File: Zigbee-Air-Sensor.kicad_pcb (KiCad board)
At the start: 4 copper layers, 34 x 45 mm, 87 parts, among them J1 USB_C_Receptacle_PowerOnly_6P, J2 Conn_01x04, J3 FH34SRJ-6S-0.5SH, J4 FH34SRJ-6S-0.5SH, J5 Conn_01x06, J6 E-Ink 24P, Q1 BC847W, Q2 CJ2101, Q3 Si1308EDL, U1 ESP32-H2-MINI-1-H4, U2 BQ25628ERYKR, U3 BQ27426YZFR, U4 TPS63030DSK, U5 SHT30-DIS, U6 LPS22DF

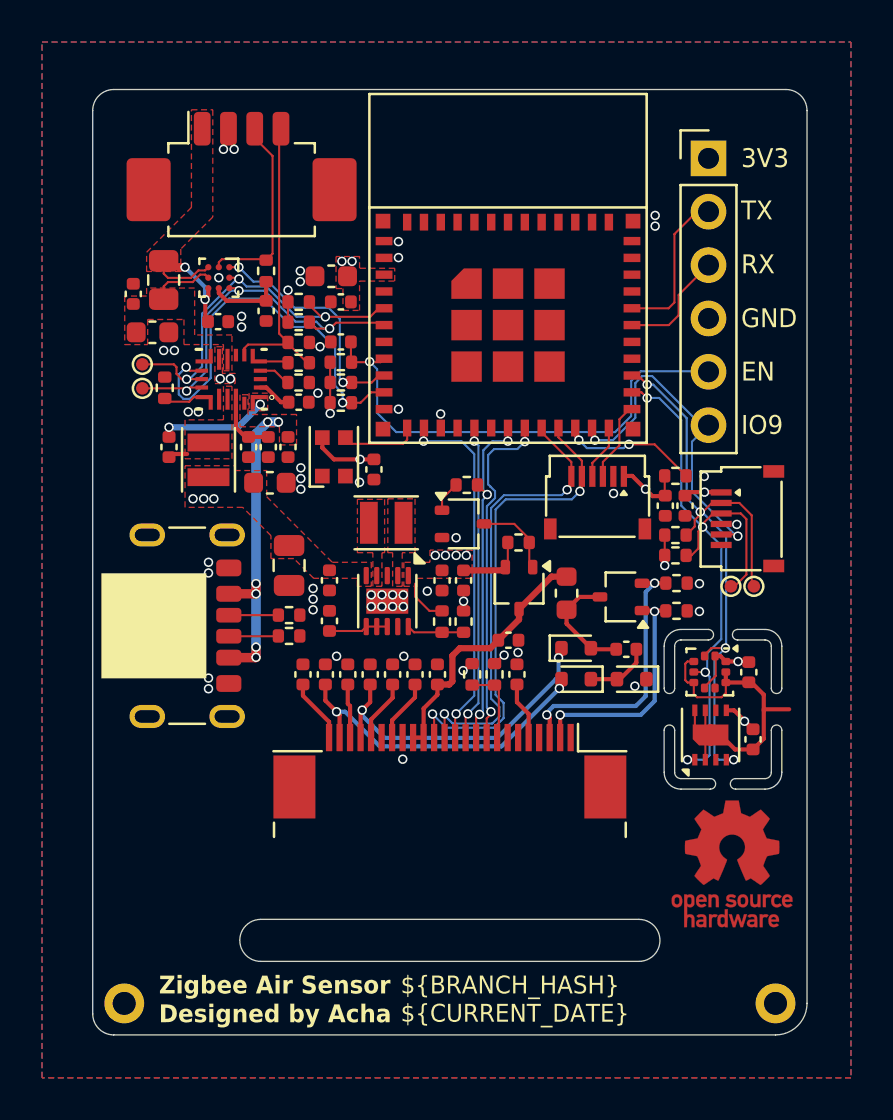
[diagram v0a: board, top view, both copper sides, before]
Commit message: Change non-plated slots to plated slots
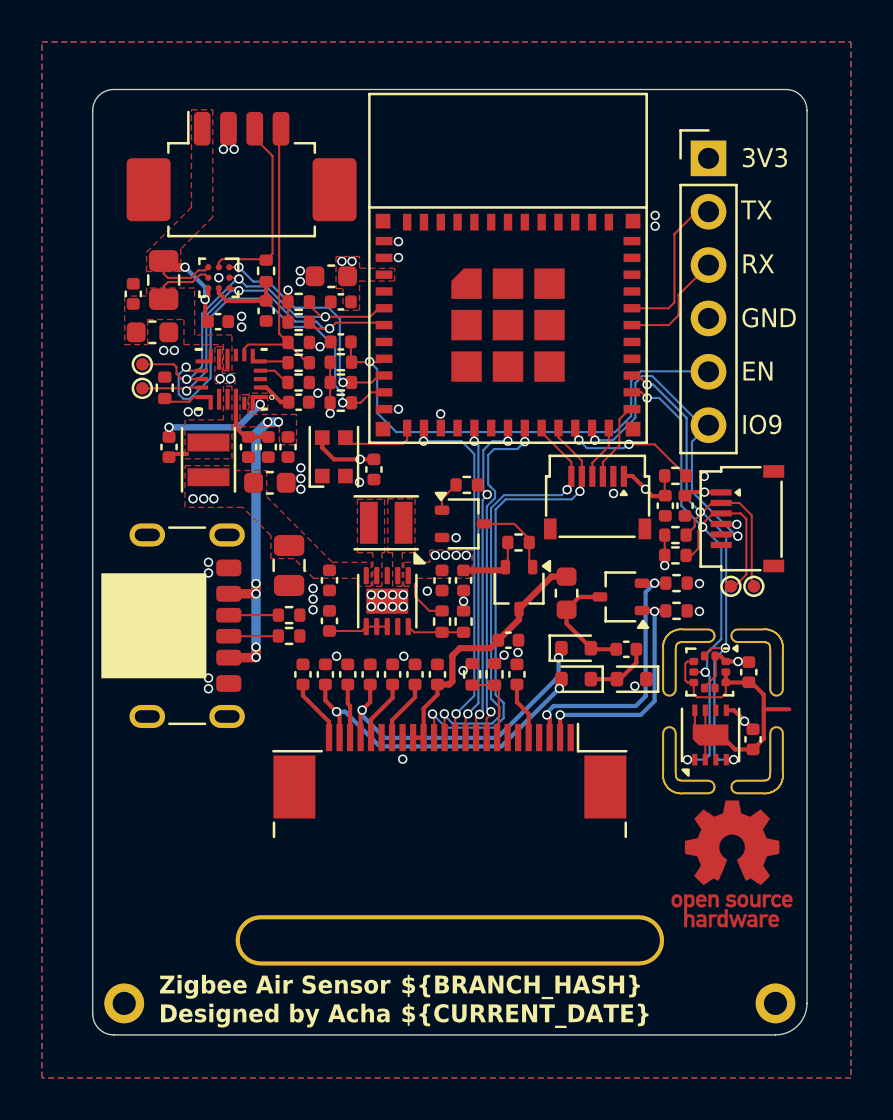
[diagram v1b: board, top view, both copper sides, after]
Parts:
- added 20.4mm_Plated_Slot: , Zigbee-Air-Sensor:20.4mm_Plated_Slot, F.Cu at (117.0, 140.5)
- added Thermal_Slot: Thermal_Slot, Zigbee-Air-Sensor:Thermal_Slot, F.Cu at (130.0, 129.6)
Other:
- outline, holes or cut-outs redrawn
- board text added: "Plated Slot"

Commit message: Adjust slot size Change GPIO assignment
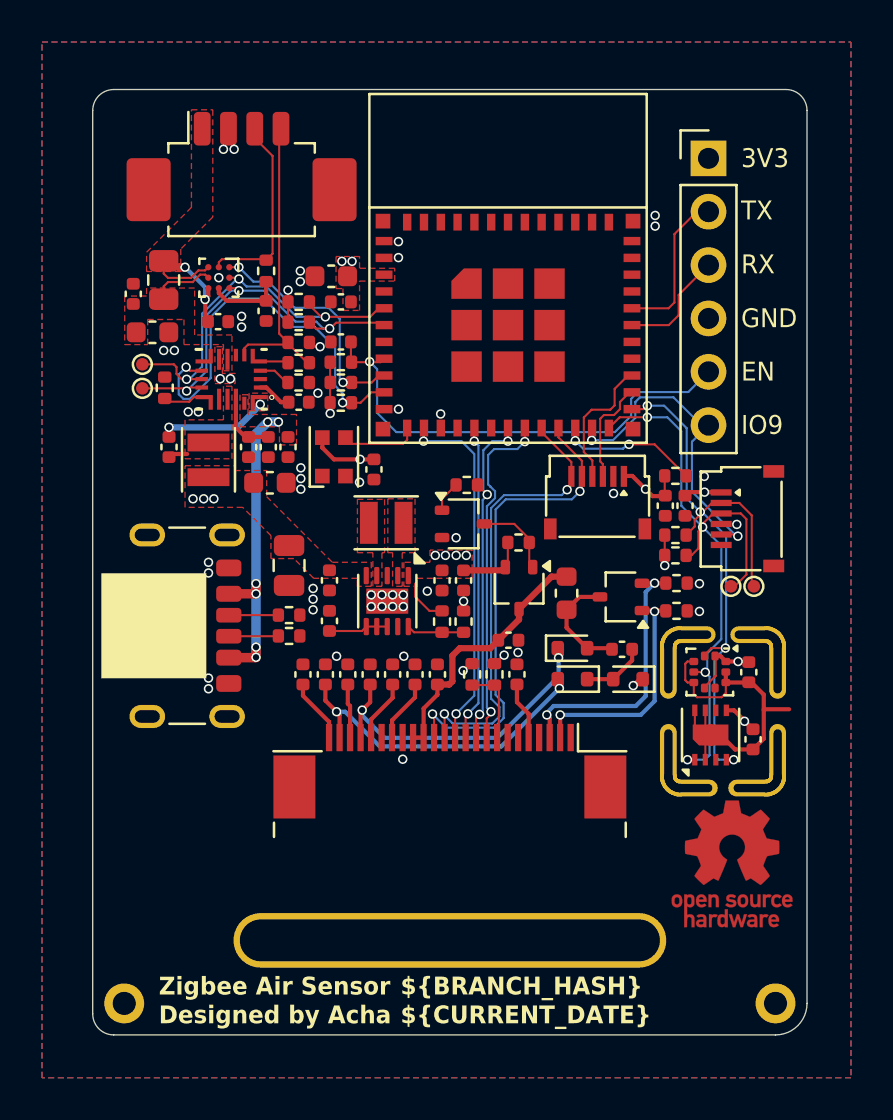
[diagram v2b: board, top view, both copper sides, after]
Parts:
- moved C23 0.20 mm to (125.2, 126.6)
- moved D2 0.18 mm to (125.5, 128.1)
- moved D3 0.18 mm to (122.8, 128.1)
- moved D4 0.18 mm to (122.8, 126.6)
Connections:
- J3 pad 3: /CS2 -> /CS2/USBD-
- J3 pad 4: /MISO -> /MISO/USBD+
- U1 pad 24: /MISO -> /Sensors/SDA
- U1 pad 25: /CS2 -> /Sensors/SCL
- U1 pad 26: /Sensors/SDA -> /CS2/USBD-
- U1 pad 27: /Sensors/SCL -> /MISO/USBD+
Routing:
- net /MISO/USBD+: track 0.00 -> 6.55 mm
- net /CS2/USBD-: track 0.00 -> 5.03 mm
- net /CS2: track 3.73 -> 0.00 mm
- net /MISO: track 2.63 -> 0.00 mm
- net /ESP32-H2/ESP32_IO9_BOOT: track 16.6 -> 15.4 mm
- net /Sensors/SCL: track 30.7 -> 29.9 mm
- net GND: track 15.8 -> 16.4 mm
- net /ESP32-H2/ESP32_EN: track 23.5 -> 23.0 mm
- net /Sensors/SDA: track 30.1 -> 30.6 mm
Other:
- board text added: "Ext.I2C"
- board text added: "Ext.SPI"
